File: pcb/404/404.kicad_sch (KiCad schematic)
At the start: 36 parts, among them J1 Conn_01x04, Q1 BC846, U1 RC4558

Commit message: [All] Add LCSC part number for JST connector
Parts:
- C1: value 22uF -> (none); footprint Capacitor_SMD:C_1206_3216Metric -> (none)
- C2, C4: value 47n -> (none); footprint Capacitor_SMD:C_0603_1608Metric -> (none)
- C3, C8: value 1uF -> (none); footprint Capacitor_SMD:C_0603_1608Metric -> (none)
- C5: value 47pF -> (none); footprint Capacitor_SMD:C_0603_1608Metric -> (none); LCSC C1671 -> C1671
- C6, C7: value 220nF -> (none); footprint Capacitor_SMD:C_0603_1608Metric -> (none)
- D1, D2, D3: value 1N4148W -> (none); footprint MeineBib:D_SOD-123+THT -> (none)
- J1: value Conn_01x04 -> (none); footprint Connector_JST:JST_XH_B4B-XH-A_1x04_P2.50mm_Vertical -> (none); LCSC (none) -> C144395
- JP1, JP2: value SolderJumper -> (none); footprint Jumper:SolderJumper-3_P1.3mm_Open_RoundedPad1.0x1.5mm_NumberLabels -> (none)
- Q1: value BC846 -> (none); footprint Package_TO_SOT_SMD:SOT-23 -> (none)
- R1, R10, R2, R5, R7: value 10K -> (none); footprint Resistor_SMD:R_0603_1608Metric -> (none)
- R11: value 220R -> (none); footprint Resistor_SMD:R_0603_1608Metric -> (none)
- R12, R3, R9: value 1K -> (none); footprint Resistor_SMD:R_0603_1608Metric -> (none)
- R4: value 510K -> (none); footprint Resistor_SMD:R_0603_1608Metric -> (none)
- R6: value 4K7 -> (none); footprint Resistor_SMD:R_0603_1608Metric -> (none)
- R8: value 51K -> (none); footprint Resistor_SMD:R_0603_1608Metric -> (none)
- RV1: value 500K -> (none); footprint Potentiometer_THT:Potentiometer_Alpha_RD901F-40-00D_Single_Vertical -> (none)
- RV2: value 20k -> (none); footprint Potentiometer_THT:Potentiometer_Alpha_RD901F-40-00D_Single_Vertical -> (none)
- RV3: value 100K -> (none); footprint Potentiometer_THT:Potentiometer_Alpha_RD901F-40-00D_Single_Vertical -> (none)
- TP1, TP2, TP3, TP4, TP5: value TP -> (none); footprint TestPoint:TestPoint_Pad_D2.0mm -> (none)
- U1: value RC4558 -> (none); footprint Package_SO:SO-8_3.9x4.9mm_P1.27mm -> (none)

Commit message: [404] Export gerbers/pos/bom
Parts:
- J1: now in the parts list
- JP1, JP2: now left out of the parts list
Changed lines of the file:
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@@
   )
   (symbol (lib_id "Connector_Generic:Conn_01x04") (at 48.26 29.21 0) (mirror x) (unit 1)
-    (in_bom no) (on_board yes)
+    (in_bom yes) (on_board yes)
     (property "Reference" "J1" (id 0) (at 51.435 29.2101 0)
       (effects (font (size 1.27 1.27)) (justify left))
@@
   )
   (symbol (lib_id "Jumper:SolderJumper_3_Open") (at 133.35 92.71 270) (unit 1)
-    (in_bom yes) (on_board yes) (fields_autoplaced)
+    (in_bom no) (on_board yes) (fields_autoplaced)
     (property "Reference" "JP2" (id 0) (at 135.89 91.4399 90)
       (effects (font (size 1.27 1.27)) (justify left))
@@
   )
   (symbol (lib_id "Jumper:SolderJumper_3_Open") (at 88.9 62.23 90) (unit 1)
-    (in_bom yes) (on_board yes) (fields_autoplaced)
+    (in_bom no) (on_board yes) (fields_autoplaced)
     (property "Reference" "JP1" (id 0) (at 86.36 60.9599 90)
       (effects (font (size 1.27 1.27)) (justify left))

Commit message: [All] Flip board to board connector on upper PCB (obstructed some silk)
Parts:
- C1: value (none) -> 22uF; footprint (none) -> Capacitor_SMD:C_1206_3216Metric
- C2, C4: value (none) -> 47n; footprint (none) -> Capacitor_SMD:C_0603_1608Metric
- C3, C8: value (none) -> 1uF; footprint (none) -> Capacitor_SMD:C_0603_1608Metric
- C5: value (none) -> 47pF; footprint (none) -> Capacitor_SMD:C_0603_1608Metric
- C6, C7: value (none) -> 220nF; footprint (none) -> Capacitor_SMD:C_0603_1608Metric
- D1, D2, D3: value (none) -> 1N4148W; footprint (none) -> MeineBib:D_SOD-123+THT
- J1: value (none) -> Conn_01x04; footprint (none) -> Connector_JST:JST_XH_B4B-XH-A_1x04_P2.50mm_Vertical
- JP1, JP2: value (none) -> SolderJumper; footprint (none) -> Jumper:SolderJumper-3_P1.3mm_Open_RoundedPad1.0x1.5mm_NumberLabels
- Q1: value (none) -> BC846; footprint (none) -> Package_TO_SOT_SMD:SOT-23
- R1, R10, R2, R5, R7: value (none) -> 10K; footprint (none) -> Resistor_SMD:R_0603_1608Metric
- R11: value (none) -> 220R; footprint (none) -> Resistor_SMD:R_0603_1608Metric
- R12, R3, R9: value (none) -> 1K; footprint (none) -> Resistor_SMD:R_0603_1608Metric
- R4: value (none) -> 510K; footprint (none) -> Resistor_SMD:R_0603_1608Metric
- R6: value (none) -> 4K7; footprint (none) -> Resistor_SMD:R_0603_1608Metric
- R8: value (none) -> 51K; footprint (none) -> Resistor_SMD:R_0603_1608Metric
- RV1: value (none) -> 500K; footprint (none) -> Potentiometer_THT:Potentiometer_Alpha_RD901F-40-00D_Single_Vertical
- RV2: value (none) -> 20k; footprint (none) -> Potentiometer_THT:Potentiometer_Alpha_RD901F-40-00D_Single_Vertical
- RV3: value (none) -> 100K; footprint (none) -> Potentiometer_THT:Potentiometer_Alpha_RD901F-40-00D_Single_Vertical
- TP1, TP2, TP3, TP4, TP5: value (none) -> TP; footprint (none) -> TestPoint:TestPoint_Pad_D2.0mm
- U1: value (none) -> RC4558; footprint (none) -> Package_SO:SO-8_3.9x4.9mm_P1.27mm
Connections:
- net +9V: now also J1.3 (Pin_3); no longer J1.2 (Pin_2)
- net GND: now also J1.4 (Pin_4); no longer J1.1 (Pin_1)
- net Upper_PCB_Input: now also J1.1 (Pin_1); no longer J1.4 (Pin_4)
- net Upper_PCB_Output: now also J1.2 (Pin_2); no longer J1.3 (Pin_3)

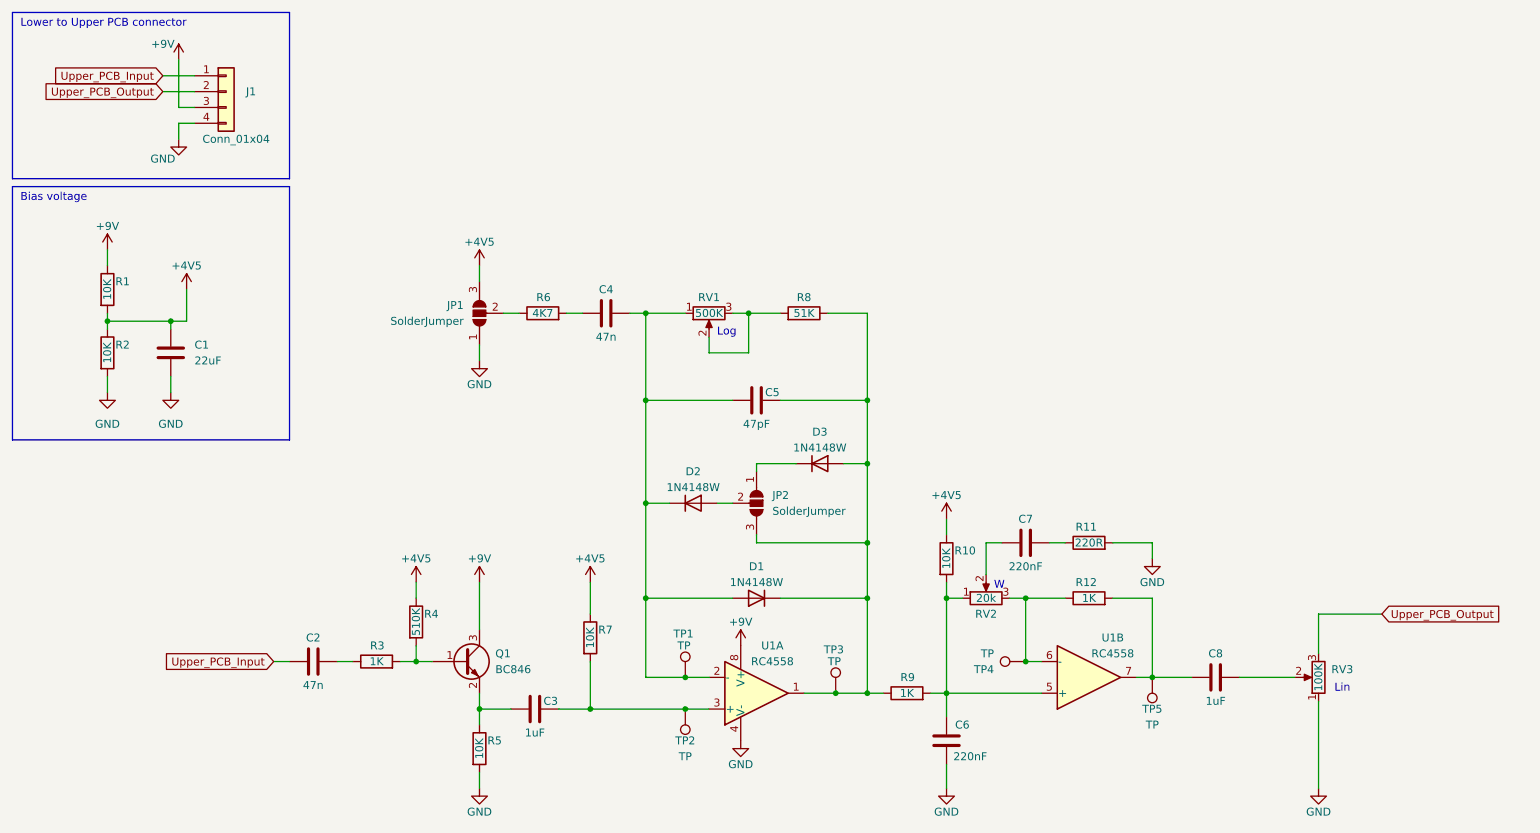
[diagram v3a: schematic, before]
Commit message: [404][UpperRaw] Apply learned lessons from TOP:
- Name on silk etc. is now a text variable
- Optimized copypasta parts
- Set pot footprint to my modified one
- Rename pots ro always be RV1-6
- Use text variables for pot names
- Show pot values on silk
- Update board constraints to JLCPCB capabilities
- Add Gndpour to UpperRaw
- Set "Not in schematic" for OSHW logo
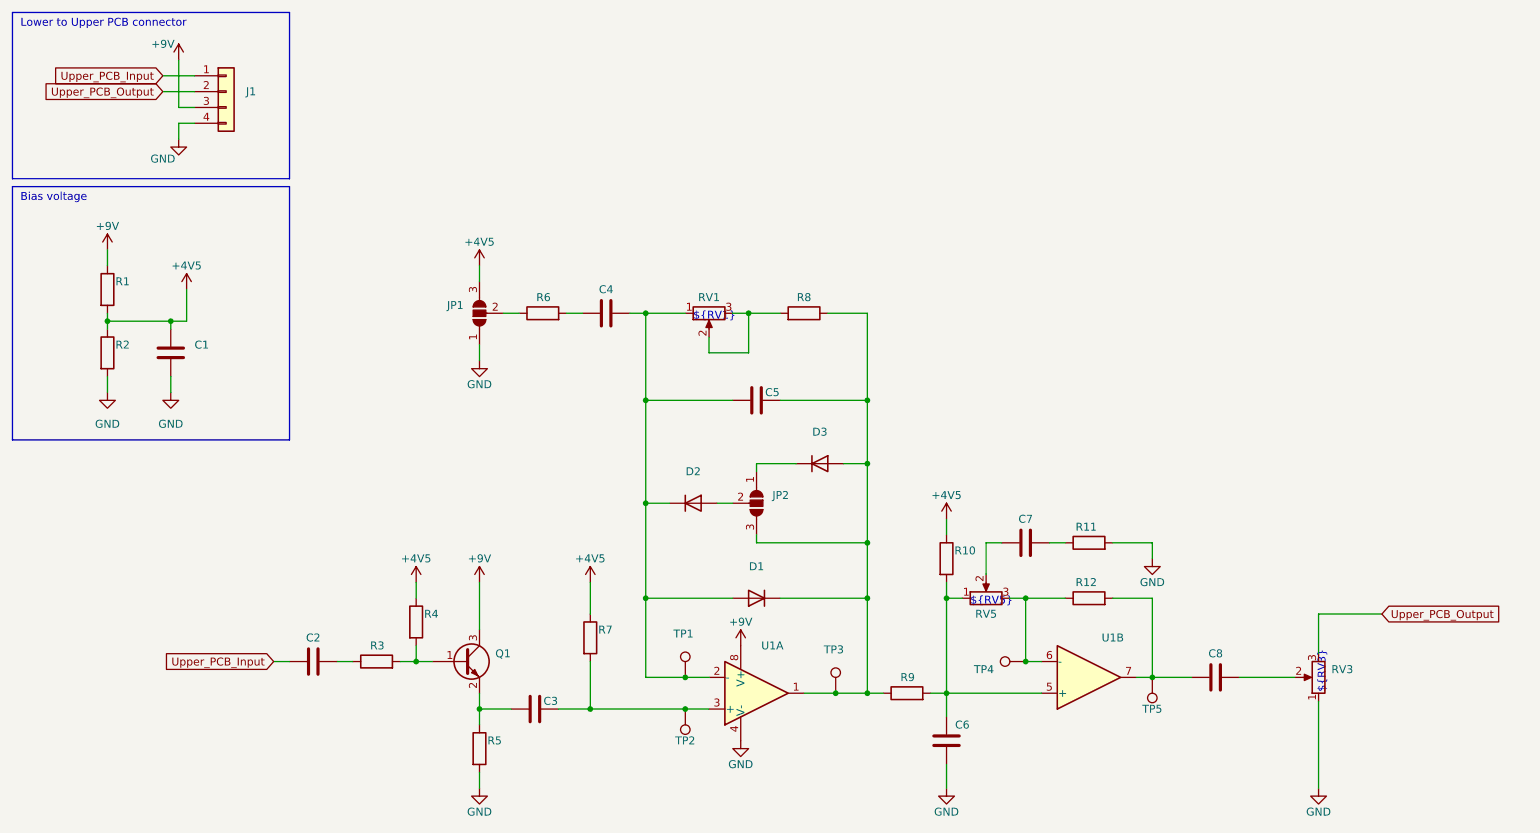
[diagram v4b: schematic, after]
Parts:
- C1: value 22uF -> (none); footprint Capacitor_SMD:C_1206_3216Metric -> (none)
- C2, C4: value 47n -> (none); footprint Capacitor_SMD:C_0603_1608Metric -> (none)
- C3, C8: value 1uF -> (none); footprint Capacitor_SMD:C_0603_1608Metric -> (none)
- C5: value 47pF -> (none); footprint Capacitor_SMD:C_0603_1608Metric -> (none)
- C6, C7: value 220nF -> (none); footprint Capacitor_SMD:C_0603_1608Metric -> (none)
- D1, D2, D3: value 1N4148W -> (none); footprint MeineBib:D_SOD-123+THT -> (none)
- J1: value Conn_01x04 -> (none); footprint Connector_JST:JST_XH_B4B-XH-A_1x04_P2.50mm_Vertical -> (none)
- JP1, JP2: value SolderJumper -> (none); footprint Jumper:SolderJumper-3_P1.3mm_Open_RoundedPad1.0x1.5mm_NumberLabels -> (none)
- Q1: value BC846 -> (none); footprint Package_TO_SOT_SMD:SOT-23 -> (none)
- R1, R10, R2, R5, R7: value 10K -> (none); footprint Resistor_SMD:R_0603_1608Metric -> (none)
- R11: value 220R -> (none); footprint Resistor_SMD:R_0603_1608Metric -> (none)
- R12, R3, R9: value 1K -> (none); footprint Resistor_SMD:R_0603_1608Metric -> (none)
- R4: value 510K -> (none); footprint Resistor_SMD:R_0603_1608Metric -> (none)
- R6: value 4K7 -> (none); footprint Resistor_SMD:R_0603_1608Metric -> (none)
- R8: value 51K -> (none); footprint Resistor_SMD:R_0603_1608Metric -> (none)
- RV1: value 500K -> (none); footprint Potentiometer_THT:Potentiometer_Alpha_RD901F-40-00D_Single_Vertical -> (none)
- RV3: value 100K -> (none); footprint Potentiometer_THT:Potentiometer_Alpha_RD901F-40-00D_Single_Vertical -> (none)
- RV5: renamed from RV2; value 20k -> (none); footprint Potentiometer_THT:Potentiometer_Alpha_RD901F-40-00D_Single_Vertical -> (none)
- TP1, TP2, TP3, TP4, TP5: value TP -> (none); footprint TestPoint:TestPoint_Pad_D2.0mm -> (none)
- U1: value RC4558 -> (none); footprint Package_SO:SO-8_3.9x4.9mm_P1.27mm -> (none)
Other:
- note added: "${RV1}"
- note added: "${RV3}"
- note added: "${RV5}"
- note removed: "Lin"
- note removed: "Log"
- note removed: "W"
